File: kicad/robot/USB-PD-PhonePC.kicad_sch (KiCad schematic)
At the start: 42 parts, among them IC1 TPS61253AYFFR, U11 MAX77958EWV+T, U15 ESD122DMYR, U16 fpf1048bucx

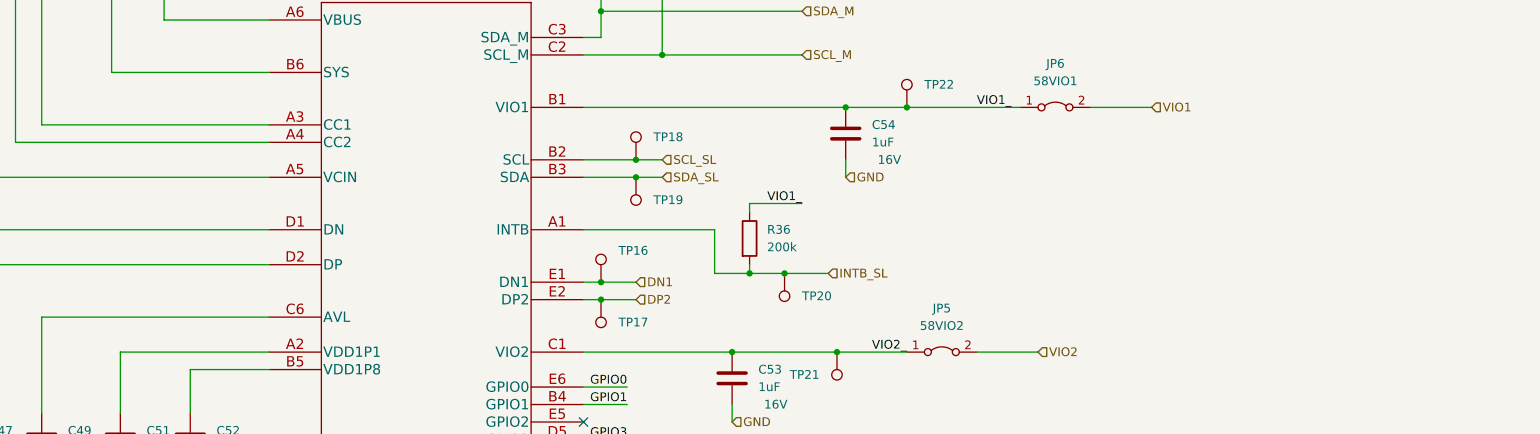
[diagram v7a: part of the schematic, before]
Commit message: Attached DP/DN pins to switch for debugging later.
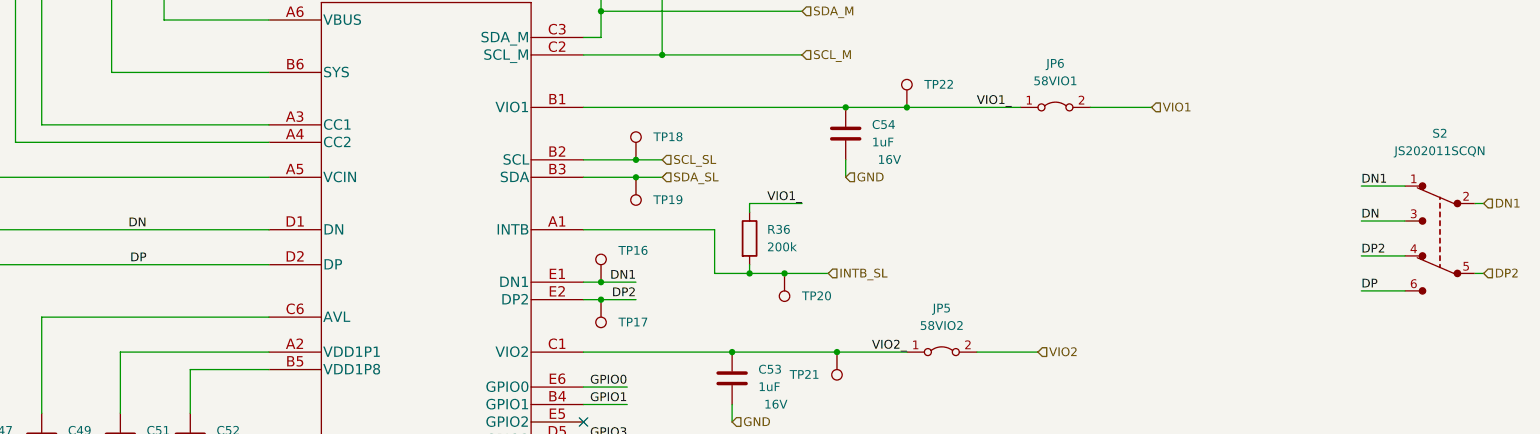
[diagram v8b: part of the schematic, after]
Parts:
- added S2: JS202011SCQN, digikey-footprints:Switch_Slide_JS202011SCQN, symbol dk_Slide-Switches:JS202011SCQN
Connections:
- net DN: now also R32.2, U11.D1 (DN), S2.3
- net DN1: now also S2.1, S2.2
- net DP: now also R33.2, U11.D2 (DP), S2.6
- net DP2: now also S2.4, S2.5
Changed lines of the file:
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@@
+    (stroke (width 0) (type default) (color 0 0 0 0))
+  )
+  (wire (pts (xy 422.91 227.33) (xy 429.26 227.33))
     (stroke (width 0) (type default) (color 0 0 0 0))
   )
@@
     (stroke (width 0) (type default) (color 0 0 0 0))
   )
+  (wire (pts (xy 440.69 224.79) (xy 439.42 224.79))
+    (stroke (width 0) (type default) (color 0 0 0 0))
+  )
   (wire (pts (xy 328.93 234.95) (xy 334.01 234.95))
     (stroke (width 0) (type default) (color 0 0 0 0))
@@
     (stroke (width 0) (type default) (color 0 0 0 0))
   )
+  (wire (pts (xy 422.91 232.41) (xy 429.26 232.41))
+    (stroke (width 0) (type default) (color 0 0 0 0))
+  )
   (wire (pts (xy 231.14 267.97) (xy 236.22 267.97))
     (stroke (width 0) (type default) (color 0 0 0 0))
@@
     (stroke (width 0) (type default) (color 0 0 0 0))
   )
+  (wire (pts (xy 422.91 237.49) (xy 429.26 237.49))
+    (stroke (width 0) (type default) (color 0 0 0 0))
+  )
   (wire (pts (xy 252.73 267.97) (xy 242.57 267.97))
     (stroke (width 0) (type default) (color 0 0 0 0))
@@
     (stroke (width 0) (type default) (color 0 0 0 0))
   )
+  (wire (pts (xy 440.69 234.95) (xy 439.42 234.95))
+    (stroke (width 0) (type default) (color 0 0 0 0))
+  )
   (wire (pts (xy 334.01 224.79) (xy 334.01 226.06))
     (stroke (width 0) (type default) (color 0 0 0 0))
@@
   )
   (wire (pts (xy 309.88 261.62) (xy 316.23 261.62))
+    (stroke (width 0) (type default) (color 0 0 0 0))
+  )
+  (wire (pts (xy 422.91 222.25) (xy 429.26 222.25))
     (stroke (width 0) (type default) (color 0 0 0 0))
   )
@@
     (effects (font (size 1.27 1.27)) (justify right bottom))
   )
+  (label "DN1" (at 422.91 222.25 0)
+    (effects (font (size 1.27 1.27)) (justify left bottom))
+  )
+  (label "DP" (at 246.38 233.68 180)
+    (effects (font (size 1.27 1.27)) (justify right bottom))
+  )
+  (label "DN1" (at 317.5 236.22 180)
+    (effects (font (size 1.27 1.27)) (justify right bottom))
+  )
   (label "GPIO4" (at 287.02 137.16 180)
     (effects (font (size 1.27 1.27)) (justify right bottom))
   )
+  (label "DN" (at 422.91 227.33 0)
+    (effects (font (size 1.27 1.27)) (justify left bottom))
+  )
   (label "GPIO0" (at 330.2 280.67 0)
     (effects (font (size 1.27 1.27)) (justify left bottom))
   )
+  (label "DP2" (at 422.91 232.41 0)
+    (effects (font (size 1.27 1.27)) (justify left bottom))
+  )
   (label "GPIO0" (at 316.23 251.46 180)
     (effects (font (size 1.27 1.27)) (justify right bottom))
@@
     (effects (font (size 1.27 1.27)) (justify right bottom))
   )
+  (label "DP" (at 422.91 237.49 0)
+    (effects (font (size 1.27 1.27)) (justify left bottom))
+  )
   (label "VIO2_" (at 312.42 177.8 0)
     (effects (font (size 1.27 1.27)) (justify left bottom))
@@
     (effects (font (size 1.27 1.27)) (justify left bottom))
   )
+  (label "DN" (at 246.38 228.6 180)
+    (effects (font (size 1.27 1.27)) (justify right bottom))
+  )
   (label "GPIO5" (at 316.23 264.16 180)
     (effects (font (size 1.27 1.27)) (justify right bottom))
@@
     (effects (font (size 1.27 1.27)) (justify right bottom))
   )
+  (label "DP2" (at 317.5 238.76 180)
+    (effects (font (size 1.27 1.27)) (justify right bottom))
+  )
   (hierarchical_label "VIO2" (shape input) (at 321.31 143.51 180)
     (effects (font (size 1.27 1.27)) (justify right))
@@
     (effects (font (size 1.27 1.27)) (justify left))
   )
-  (hierarchical_label "DN1" (shape input) (at 317.5 236.22 0)
+  (hierarchical_label "DN1" (shape input) (at 440.69 224.79 0)
     (effects (font (size 1.27 1.27)) (justify left))
   )
@@
     (effects (font (size 1.27 1.27)) (justify left))
   )
-  (hierarchical_label "DP2" (shape input) (at 317.5 238.76 0)
+  (hierarchical_label "DP2" (shape input) (at 440.69 234.95 0)
     (effects (font (size 1.27 1.27)) (justify left))
   )
@@
     (pin "2")
   )
+  (symbol (lib_id "dk_Slide-Switches:JS202011SCQN") (at 434.34 229.87 0) (mirror y) (unit 1)
+    (in_bom yes) (on_board yes)
+    (property "Reference" "S2" (id 0) (at 434.34 214.63 0))
+    (property "Value" "JS202011SCQN" (id 1) (at 434.34 217.17 0))
+    (property "Footprint" "digikey-footprints:Switch_Slide_JS202011SCQN" (id 2) (at 429.26 224.79 0)
+      (effects (font (size 1.27 1.27)) (justify left) hide)
+    )
+    (property "Datasheet" "https://www.ckswitches.com/media/1422/js.pdf" (id 3) (at 429.26 222.25 0)
+      (effects (font (size 1.524 1.524)) (justify left) hide)
+    )
+    (property "Digi-Key_PN" "401-2002-1-ND" (id 4) (at 429.26 219.71 0)
+      (effects (font (size 1.524 1.524)) (justify left) hide)
+    )
+    (property "MPN" "JS202011SCQN" (id 5) (at 429.26 217.17 0)
+      (effects (font (size 1.524 1.524)) (justify left) hide)
+    )
+    (property "Category" "Switches" (id 6) (at 429.26 214.63 0)
+      (effects (font (size 1.524 1.524)) (justify left) hide)
+    )
+    (property "Family" "Slide Switches" (id 7) (at 429.26 212.09 0)
+      (effects (font (size 1.524 1.524)) (justify left) hide)
+    )
+    (property "DK_Datasheet_Link" "https://www.ckswitches.com/media/1422/js.pdf" (id 8) (at 429.26 209.55 0)
+      (effects (font (size 1.524 1.524)) (justify left) hide)
+    )
+    (property "DK_Detail_Page" "/product-detail/en/c-k/JS202011SCQN/401-2002-1-ND/1640098" (id 9) (at 429.26 207.01 0)
+      (effects (font (size 1.524 1.524)) (justify left) hide)
+    )
+    (property "Description" "SWITCH SLIDE DPDT 300MA 6V" (id 10) (at 429.26 204.47 0)
+      (effects (font (size 1.524 1.524)) (justify left) hide)
+    )
+    (property "Manufacturer" "C&K" (id 11) (at 429.26 201.93 0)
+      (effects (font (size 1.524 1.524)) (justify left) hide)
+    )
+    (property "Status" "Active" (id 12) (at 429.26 199.39 0)
+      (effects (font (size 1.524 1.524)) (justify left) hide)
+    )
+    (pin "1")
+    (pin "2")
+    (pin "3")
+    (pin "4")
+    (pin "5")
+    (pin "6")
+  )
   (symbol (lib_id "Device:C") (at 331.47 250.19 0) (unit 1)
